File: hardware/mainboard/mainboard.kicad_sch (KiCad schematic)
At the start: 0 parts

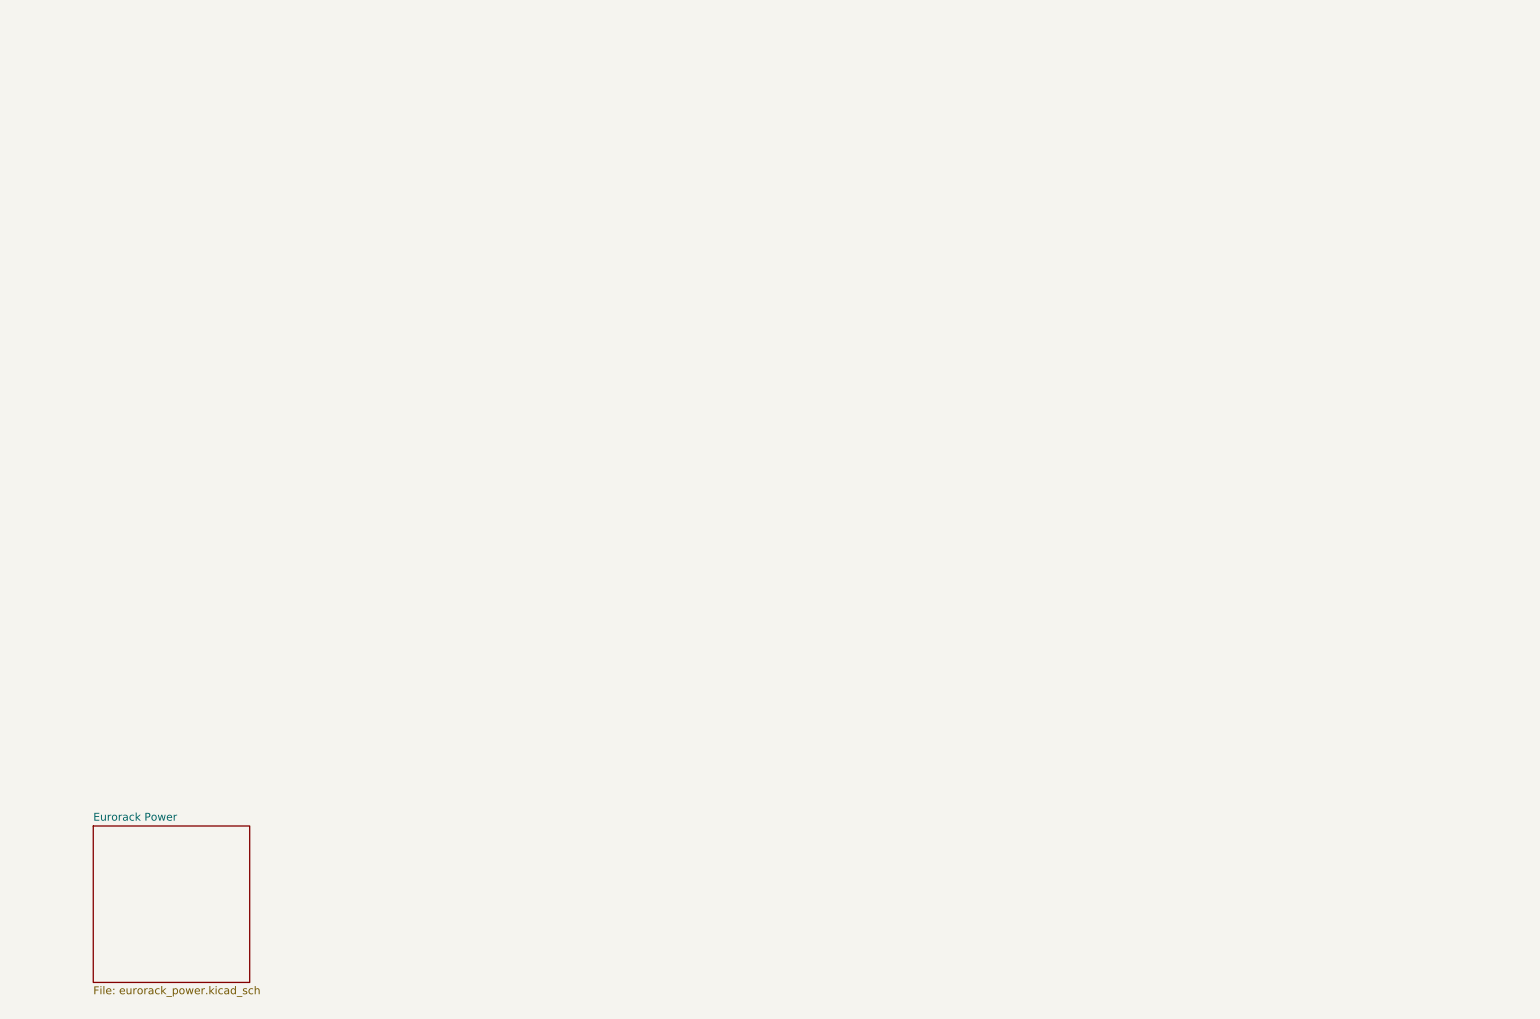
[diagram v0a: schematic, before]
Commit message: Add mixer circuitry
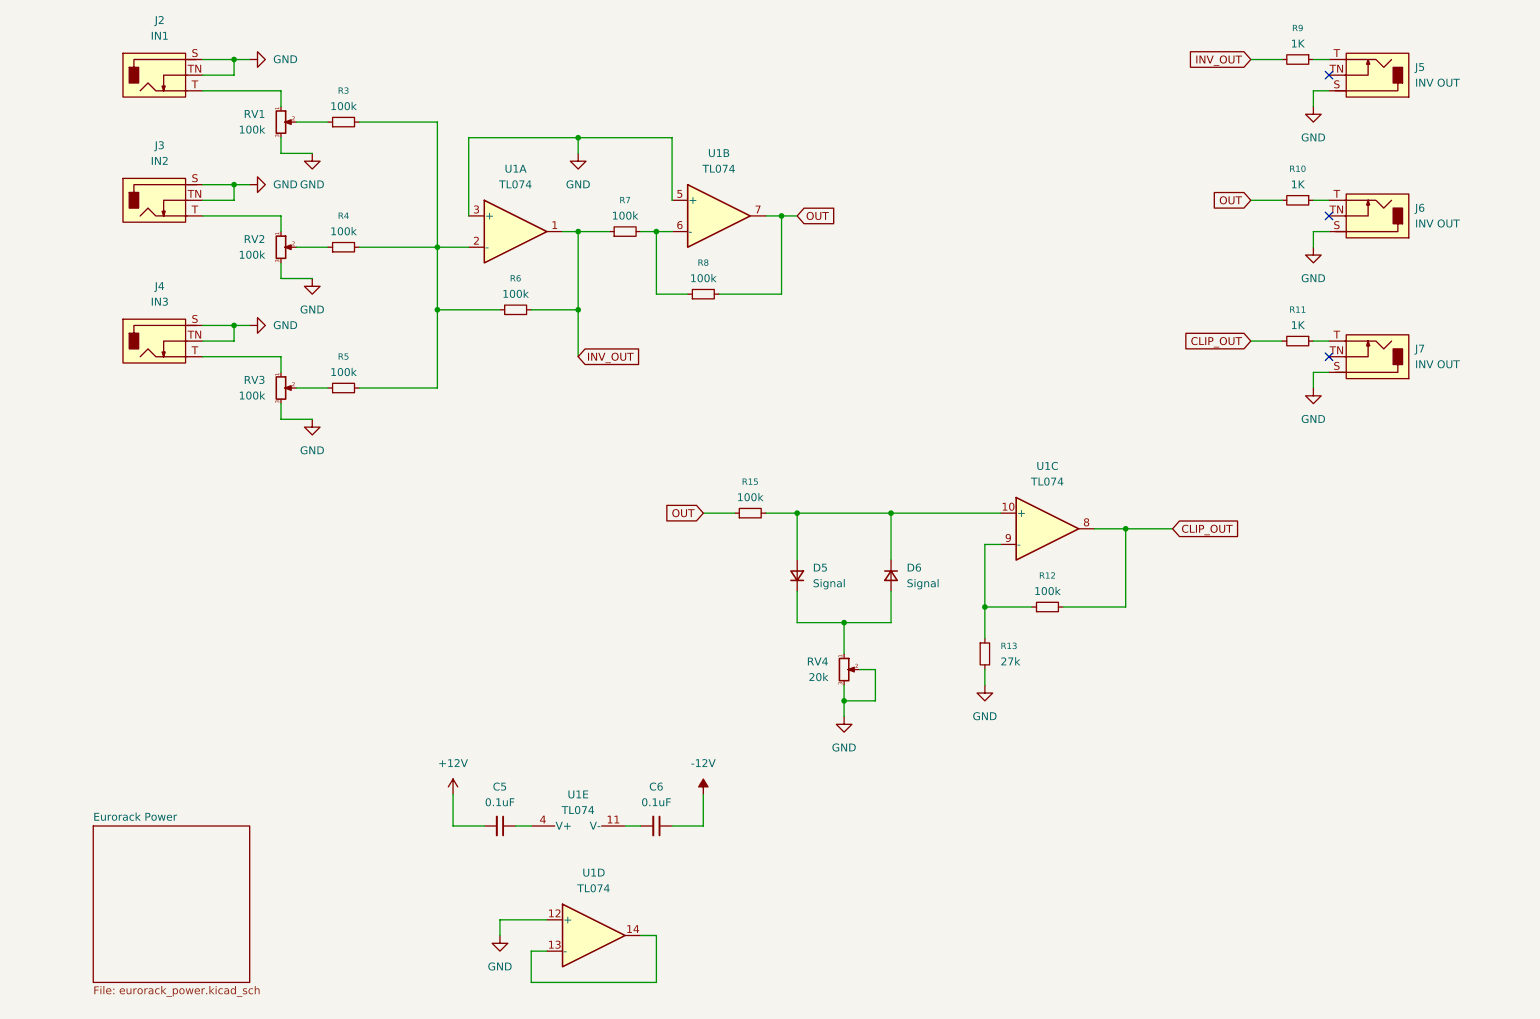
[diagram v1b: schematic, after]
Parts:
- added C5, C6: 0.1uF, symbol Device:C_Small
- added D5, D6: Signal, symbol Device:D_Small
- added J2: IN1, symbol Eurorack:PJ398
- added J3: IN2, symbol Eurorack:PJ398
- added J4: IN3, symbol Eurorack:PJ398
- added J5, J6, J7: INV OUT, symbol Eurorack:PJ398
- added R10, R11, R9: 1K, symbol Device:R_Small
- added R12, R15, R3, R4, R5, R6, R7, R8: 100k, symbol Device:R_Small
- added R13: 27k, symbol Device:R_Small
- added RV1, RV2, RV3: 100k, symbol Device:R_Potentiometer_Small
- added RV4: 20k, symbol Device:R_Potentiometer_Small
- added U1: TL074, symbol Amplifier_Operational:TL074
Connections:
- new net: D5.1 (K), D6.2 (A), RV4.1
- new net: D5.2 (A), D6.1 (K), R15.2, U1.10 (+)
- new net: C6.2, U1.11 (V-)
- new net: C5.1, U1.4 (V+)
- new net: J6.T, R10.1
- new net: R4.1, RV2.2
- new net: R3.2, R4.2, R5.2, R6.1, U1.2 (-)
- new net: R3.1, RV1.2
- new net: J3.T, RV2.1
- new net: R7.2, R8.1, U1.6 (-)
- new net: J7.T, R11.1
- new net: J5.T, R9.1
- new net: R12.1, R13.1, U1.9 (-)
- new net: U1.13 (-), U1.14
- new net: J4.T, RV3.1
- new net: J2.T, RV1.1
- new net: R5.1, RV3.2
- new net +12V: C5.2
- new net -12V: C6.1
- new net CLIP_OUT: R11.2, R12.2, U1.8
- new net GND: J2.S, J2.TN, J3.S, J3.TN, J4.S, J4.TN, J5.S, J6.S, J7.S, R13.2, RV1.3, RV2.3, RV3.3, RV4.2, RV4.3, U1.12 (+), U1.3 (+), U1.5 (+)
- new net INV_OUT: R6.2, R7.1, R9.2, U1.1
- new net OUT: R10.2, R15.1, R8.2, U1.7
- no-connect marks 0 -> 3

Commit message: Add footprints
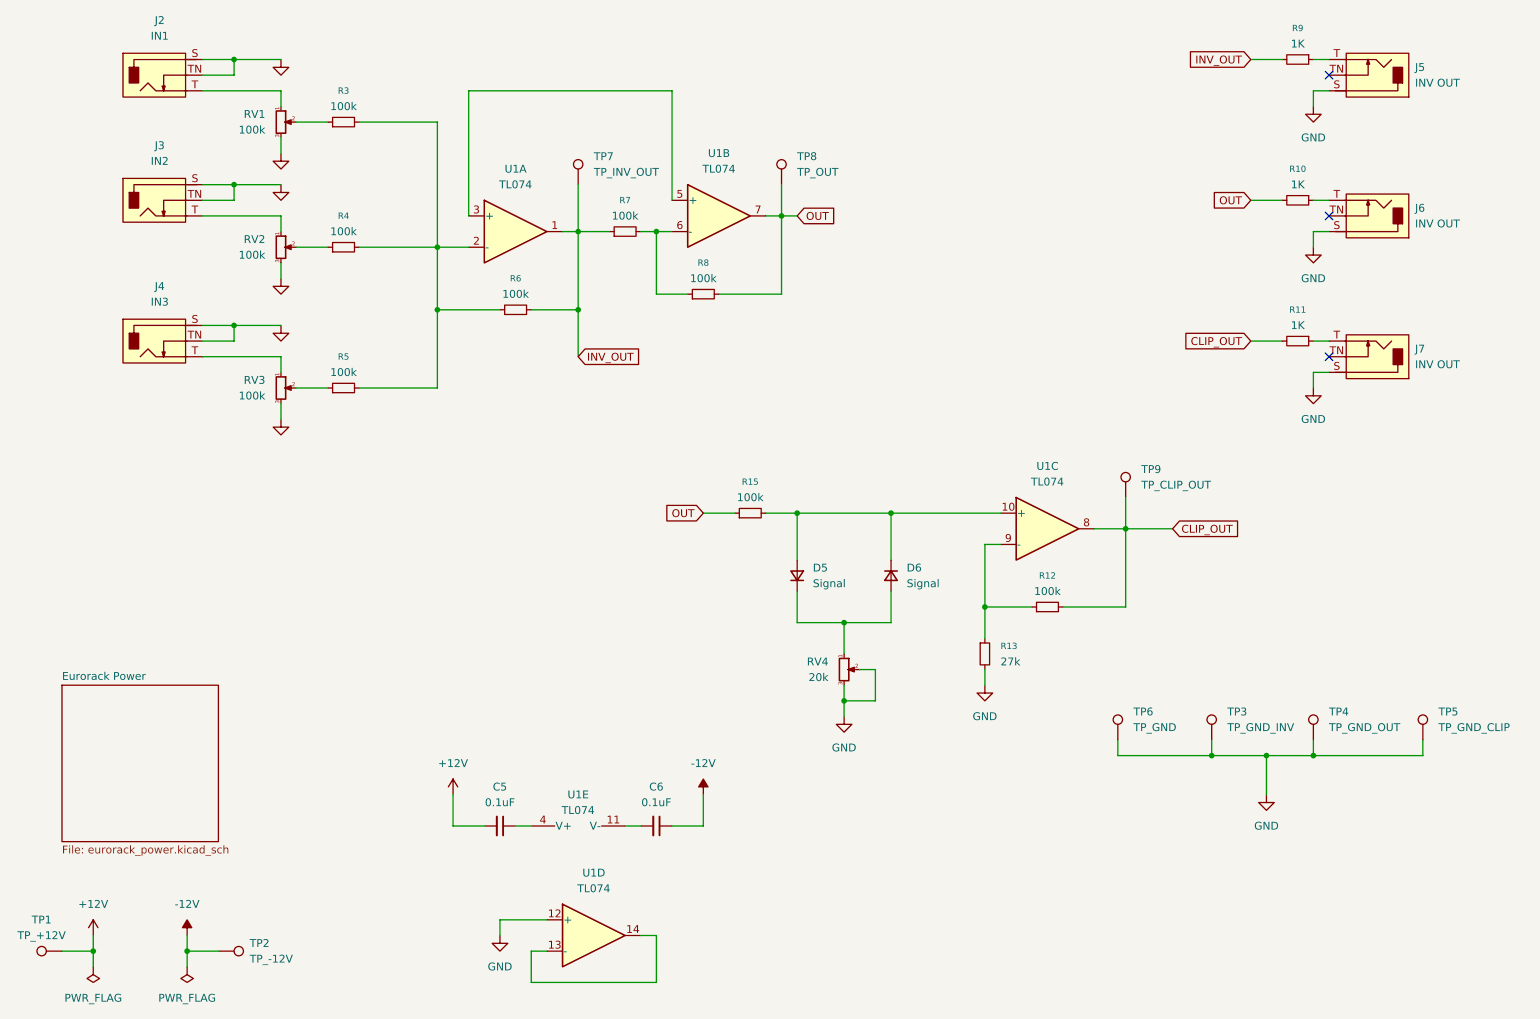
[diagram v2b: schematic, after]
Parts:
- added TP1: TP_+12V, TestPoint:TestPoint_Keystone_5000-5004_Miniature, symbol Connector:TestPoint
- added TP2: TP_-12V, TestPoint:TestPoint_Keystone_5000-5004_Miniature, symbol Connector:TestPoint
- added TP3: TP_GND_INV, TestPoint:TestPoint_Keystone_5000-5004_Miniature, symbol Connector:TestPoint
- added TP4: TP_GND_OUT, TestPoint:TestPoint_Keystone_5000-5004_Miniature, symbol Connector:TestPoint
- added TP5: TP_GND_CLIP, TestPoint:TestPoint_Keystone_5000-5004_Miniature, symbol Connector:TestPoint
- added TP6: TP_GND, TestPoint:TestPoint_Keystone_5000-5004_Miniature, symbol Connector:TestPoint
- added TP7: TP_INV_OUT, TestPoint:TestPoint_Keystone_5000-5004_Miniature, symbol Connector:TestPoint
- added TP8: TP_OUT, TestPoint:TestPoint_Keystone_5000-5004_Miniature, symbol Connector:TestPoint
- added TP9: TP_CLIP_OUT, TestPoint:TestPoint_Keystone_5000-5004_Miniature, symbol Connector:TestPoint
- C5, C6: footprint (none) -> Capacitor_SMD:C_0805_2012Metric_Pad1.18x1.45mm_HandSolder
- D5, D6: footprint (none) -> Diode_SMD:D_SOD-123
- J2, J3, J4, J5, J6, J7: footprint (none) -> Connector_Audio:Jack_3.5mm_QingPu_WQP-PJ398SM_Vertical_CircularHoles
- R10, R11, R12, R13, R15, R3, R4, R5, R6, R7, R8, R9: footprint (none) -> Resistor_SMD:R_0805_2012Metric_Pad1.20x1.40mm_HandSolder
- RV1, RV2, RV3: footprint (none) -> Potentiometer_THT:Potentiometer_Alpha_RD901F-40-00D_Single_Vertical
- RV4: footprint (none) -> Potentiometer_SMD:Potentiometer_Bourns_3224W_Vertical
- U1: footprint (none) -> Package_SO:SOIC-14_3.9x8.7mm_P1.27mm
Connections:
- net +12V: now also TP1.1
- net -12V: now also TP2.1
- net CLIP_OUT: now also TP9.1
- net GND: now also TP3.1, TP4.1, TP5.1, TP6.1; no longer U1.3 (+), U1.5 (+)
- net INV_OUT: now also TP7.1
- net OUT: now also TP8.1
- new net: U1.3 (+), U1.5 (+)

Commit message: Layout
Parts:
- removed TP4: TP_GND_OUT, TestPoint:TestPoint_Keystone_5000-5004_Miniature, symbol Connector:TestPoint
- removed TP6: TP_GND, TestPoint:TestPoint_Keystone_5000-5004_Miniature, symbol Connector:TestPoint
- J2, J3, J4, J5: footprint Connector_Audio:Jack_3.5mm_QingPu_WQP-PJ398SM_Vertical_CircularHoles -> EurorackFootprints:Jack_3.5mm_WQP-PJ398SM_Vertical_Tight
- J6: value INV OUT -> OUT; footprint Connector_Audio:Jack_3.5mm_QingPu_WQP-PJ398SM_Vertical_CircularHoles -> EurorackFootprints:Jack_3.5mm_WQP-PJ398SM_Vertical_Tight
- J7: value INV OUT -> CLIP OUT; footprint Connector_Audio:Jack_3.5mm_QingPu_WQP-PJ398SM_Vertical_CircularHoles -> EurorackFootprints:Jack_3.5mm_WQP-PJ398SM_Vertical_Tight
- TP3: value TP_GND_INV -> TP_GND
- TP5: value TP_GND_CLIP -> TP_GND
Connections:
- net +12V: now also C5.1, U1.4 (V+); no longer C5.2
- net -12V: now also U1.11 (V-)
- net GND: now also C5.2, C6.2, U1.3 (+), U1.5 (+)
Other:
- moved on the sheet: C5, C6, TP5, U1D, U1E

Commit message: Clean up
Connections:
- net CLIP_DIODES: now reaches D5.2 (A), D6.1 (K), R15.2, U1.10 (+)
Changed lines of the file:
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@@
 	)
 	(junction
+		(at 161.29 109.22)
+		(diameter 0)
+		(color 0 0 0 0)
+	)
+	(junction
 		(at 66.04 55.88)
 		(diameter 0)
@@
 	)
 	(junction
-		(at 157.48 109.22)
+		(at 228.6 151.13)
 		(diameter 0)
 		(color 0 0 0 0)
 	)
 	(junction
-		(at 233.68 151.13)
+		(at 157.48 109.22)
 		(diameter 0)
 		(color 0 0 0 0)
@@
 	(wire
 		(pts
-			(xy 233.68 151.13) (xy 233.68 154.94)
+			(xy 228.6 151.13) (xy 228.6 156.21)
 		)
 		(stroke
@@
 	(wire
 		(pts
-			(xy 157.48 109.22) (xy 172.72 109.22)
+			(xy 157.48 109.22) (xy 161.29 109.22)
 		)
 		(stroke
@@
 	(wire
 		(pts
+			(xy 161.29 109.22) (xy 172.72 109.22)
+		)
+		(stroke
+			(width 0)
+			(type default)
+		)
+	)
+	(wire
+		(pts
 			(xy 99.06 66.04) (xy 104.14 66.04)
 		)
@@
 	(wire
 		(pts
-			(xy 222.25 151.13) (xy 233.68 151.13)
+			(xy 222.25 151.13) (xy 228.6 151.13)
 		)
 		(stroke
@@
 	(wire
 		(pts
+			(xy 161.29 105.41) (xy 161.29 109.22)
+		)
+		(stroke
+			(width 0)
+			(type default)
+		)
+	)
+	(wire
+		(pts
 			(xy 60.96 81.28) (xy 66.04 81.28)
 		)
@@
 	(wire
 		(pts
+			(xy 163.83 105.41) (xy 161.29 105.41)
+		)
+		(stroke
+			(width 0)
+			(type default)
+		)
+	)
+	(wire
+		(pts
+			(xy 228.6 151.13) (xy 233.68 151.13)
+		)
+		(stroke
+			(width 0)
+			(type default)
+		)
+	)
+	(wire
+		(pts
 			(xy 60.96 78.74) (xy 66.04 78.74)
 		)
@@
 		)
 	)
+	(global_label "CLIP_DIODES"
+		(shape input)
+		(at 163.83 105.41 0)
+		(fields_autoplaced yes)
+		(effects
+			(font
+				(size 1.27 1.27)
+			)
+			(justify left)
+		)
+		(property "Intersheetrefs" "${INTERSHEET_REFS}"
+			(at 178.7895 105.41 0)
+			(effects
+				(font
+					(size 1.27 1.27)
+				)
+				(justify left)
+				(hide yes)
+			)
+		)
+	)
 	(global_label "INV_OUT"
 		(shape input)
@@
 	(symbol
 		(lib_id "power:GND")
-		(at 233.68 154.94 0)
+		(at 228.6 156.21 0)
 		(unit 1)
 		(exclude_from_sim no)
@@
 		(fields_autoplaced yes)
 		(property "Reference" "#PWR025"
-			(at 233.68 161.29 0)
+			(at 228.6 162.56 0)
 			(effects
 				(font
@@
 		)
 		(property "Value" "GND"
-			(at 233.68 160.02 0)
+			(at 228.6 161.29 0)
 			(effects
 				(font
@@
 		)
 		(property "Footprint" ""
-			(at 233.68 154.94 0)
+			(at 228.6 156.21 0)
 			(effects
 				(font
@@
 		)
 		(property "Datasheet" ""
-			(at 233.68 154.94 0)
+			(at 228.6 156.21 0)
 			(effects
 				(font
@@
 		)
 		(property "Description" "Power symbol creates a global label with name \"GND\" , ground"
-			(at 233.68 154.94 0)
+			(at 228.6 156.21 0)
 			(effects
 				(font

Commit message: Sent mainboard
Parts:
- C5, C6: LCSC_Part_No (none) -> C49678; Manufacturer (none) -> YAGEO; Manufacturer_Part_No (none) -> CC0805KRX7R9BB104
- D5, D6: LCSC_Part_No (none) -> C82544; Manufacturer (none) -> DIODES; Manufacturer_Part_No (none) -> 1N5819HW-7-F
- J2, J3, J4, J5, J6, J7, RV1, RV2, RV3: now left out of the parts list
- R10, R11, R9: LCSC_Part_No (none) -> C17513; Manufacturer (none) -> UNI-ROYAL; Manufacturer_Part_No (none) -> 0805W8F1001T5E
- R12, R15, R3, R4, R5, R6, R7, R8: LCSC_Part_No (none) -> C149504; Manufacturer (none) -> UNI-ROYAL; Manufacturer_Part_No (none) -> 0805W8F1003T5E
- R13: LCSC_Part_No (none) -> C17593; Manufacturer (none) -> UNI-ROYAL; Manufacturer_Part_No (none) -> 0805W8F2702T5E
- RV4: LCSC_Part_No (none) -> C55071; Manufacturer (none) -> BOURNS; Manufacturer_Part_No (none) -> 3224W-1-203E
- TP1, TP2, TP3, TP5, TP7, TP8, TP9: LCSC_Part_No (none) -> C5199801; Manufacturer (none) -> ronghe; Manufacturer_Part_No (none) -> RH-5001
- U1: LCSC_Part_No (none) -> C12594; Manufacturer (none) -> TI; Manufacturer_Part_No (none) -> TL074CDR

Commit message: Updates
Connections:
- net GND: now also RV1.1, RV2.1, RV3.1; no longer RV1.3, RV2.3, RV3.3
- net at J3.T: now also RV2.3; no longer RV2.1
- net at J4.T: now also RV3.3; no longer RV3.1
- net at J2.T: now also RV1.3; no longer RV1.1
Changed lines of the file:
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@@
 	(wire
 		(pts
+			(xy 50.8 180.34) (xy 50.8 181.61)
+		)
+		(stroke
+			(width 0)
+			(type default)
+		)
+	)
+	(wire
+		(pts
 			(xy 73.66 60.96) (xy 73.66 63.5)
 		)
@@
 	)
 	(symbol
+		(lib_id "power:PWR_FLAG")
+		(at 50.8 180.34 0)
+		(unit 1)
+		(exclude_from_sim no)
+		(in_bom yes)
+		(on_board yes)
+		(dnp no)
+		(fields_autoplaced yes)
+		(property "Reference" "#FLG03"
+			(at 50.8 178.435 0)
+			(effects
+				(font
+					(size 1.27 1.27)
+				)
+				(hide yes)
+			)
+		)
+		(property "Value" "PWR_FLAG"
+			(at 50.8 175.26 0)
+			(effects
+				(font
+					(size 1.27 1.27)
+				)
+			)
+		)
+		(property "Footprint" ""
+			(at 50.8 180.34 0)
+			(effects
+				(font
+					(size 1.27 1.27)
+				)
+				(hide yes)
+			)
+		)
+		(property "Datasheet" "~"
+			(at 50.8 180.34 0)
+			(effects
+				(font
+					(size 1.27 1.27)
+				)
+				(hide yes)
+			)
+		)
+		(property "Description" "Special symbol for telling ERC where power comes from"
+			(at 50.8 180.34 0)
+			(effects
+				(font
+					(size 1.27 1.27)
+				)
+				(hide yes)
+			)
+		)
+		(pin "1"
+		)
+		(instances
+			(project ""
+				(path "/fbd7df8d-6163-4a0b-a1e8-4fc30445a118"
+					(reference "#FLG03")
+					(unit 1)
+				)
+			)
+		)
+	)
+	(symbol
 		(lib_id "power:GND")
 		(at 129.54 153.67 0)
@@
 		(lib_id "Device:R_Potentiometer_Small")
 		(at 73.66 66.04 0)
+		(mirror x)
 		(unit 1)
 		(exclude_from_sim no)
@@
 		(on_board yes)
 		(dnp no)
-		(fields_autoplaced yes)
 		(property "Reference" "RV2"
 			(at 71.12 64.7699 0)
@@
 	)
 	(symbol
+		(lib_id "power:GND")
+		(at 50.8 181.61 0)
+		(unit 1)
+		(exclude_from_sim no)
+		(in_bom yes)
+		(on_board yes)
+		(dnp no)
+		(fields_autoplaced yes)
+		(property "Reference" "#PWR032"
+			(at 50.8 187.96 0)
+			(effects
+				(font
+					(size 1.27 1.27)
+				)
+				(hide yes)
+			)
+		)
+		(property "Value" "GND"
+			(at 50.8 186.69 0)
+			(effects
+				(font
+					(size 1.27 1.27)
+				)
+			)
+		)
+		(property "Footprint" ""
+			(at 50.8 181.61 0)
+			(effects
+				(font
+					(size 1.27 1.27)
+				)
+				(hide yes)
+			)
+		)
+		(property "Datasheet" ""
+			(at 50.8 181.61 0)
+			(effects
+				(font
+					(size 1.27 1.27)
+				)
+				(hide yes)
+			)
+		)
+		(property "Description" "Power symbol creates a global label with name \"GND\" , ground"
+			(at 50.8 181.61 0)
+			(effects
+				(font
+					(size 1.27 1.27)
+				)
+				(hide yes)
+			)
+		)
+		(pin "1"
+		)
+		(instances
+			(project ""
+				(path "/fbd7df8d-6163-4a0b-a1e8-4fc30445a118"
+					(reference "#PWR032")
+					(unit 1)
+				)
+			)
+		)
+	)
+	(symbol
 		(lib_id "Device:R_Small")
 		(at 187.96 132.08 0)
@@
 		(lib_id "Device:R_Potentiometer_Small")
 		(at 73.66 88.9 0)
+		(mirror x)
 		(unit 1)
 		(exclude_from_sim no)
@@
 		(on_board yes)
 		(dnp no)
-		(fields_autoplaced yes)
 		(property "Reference" "RV3"
 			(at 71.12 87.6299 0)
@@
 		(lib_id "Device:R_Potentiometer_Small")
 		(at 73.66 45.72 0)
+		(mirror x)
 		(unit 1)
 		(exclude_from_sim no)
@@
 		(on_board yes)
 		(dnp no)
-		(fields_autoplaced yes)
 		(property "Reference" "RV1"
 			(at 71.12 44.4499 0)
